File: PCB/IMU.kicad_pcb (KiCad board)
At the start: 2 copper layers, 65 parts, among them IC1 STM32F405VGT, IC2 ADP3335ARMZ-3.3, IC3 ADP3335ARMZ-5, IC4 MS5611-01BA03, P1 UART1, P2 SWD, P3 UART2, P4 SPI, P5 BATTERY, P6 USB_OTG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

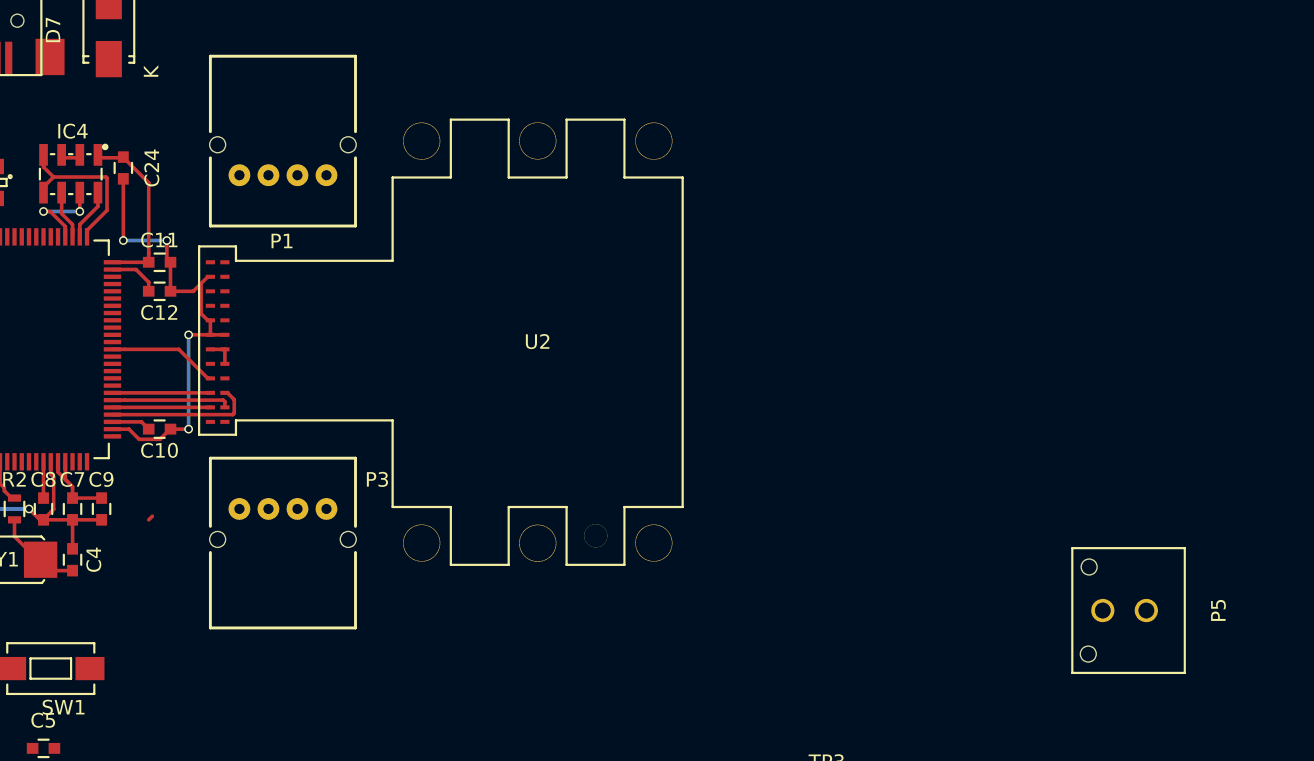
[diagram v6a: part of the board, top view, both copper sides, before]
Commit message: PCB: re-import netlist with new footprints
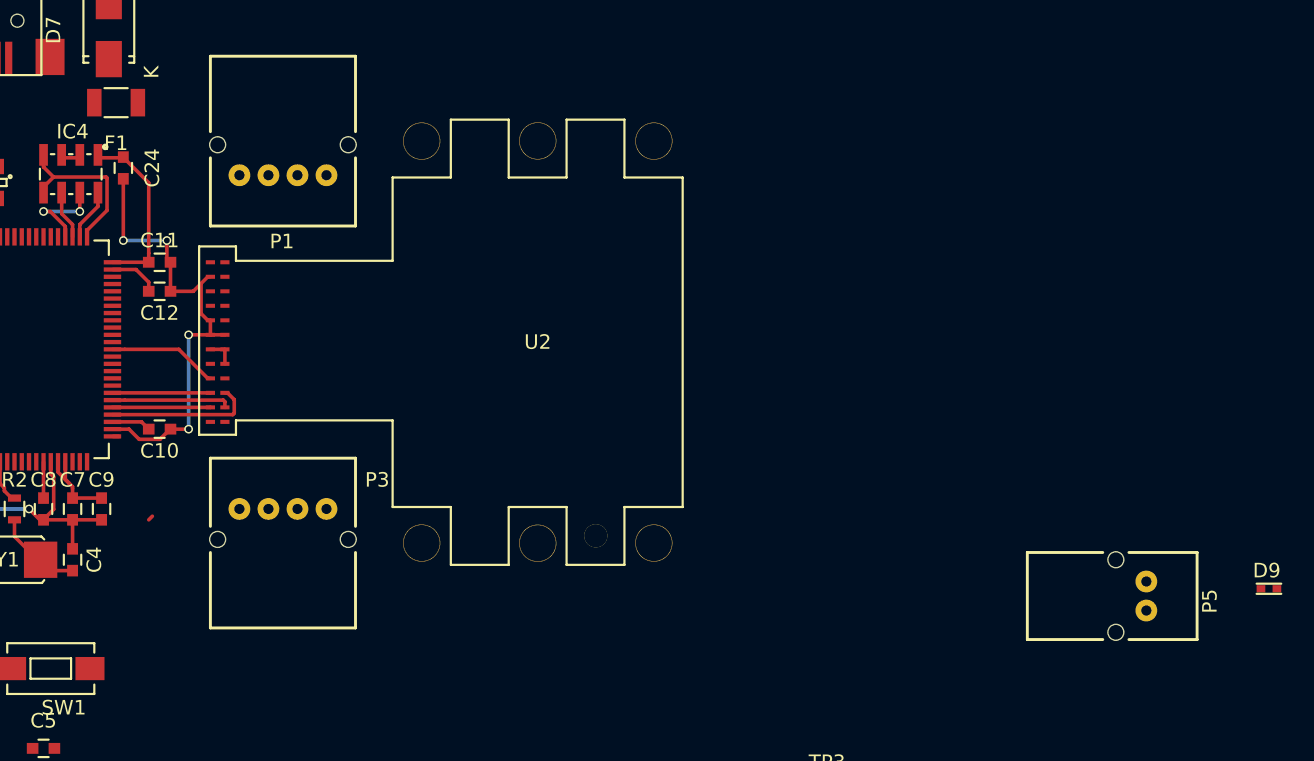
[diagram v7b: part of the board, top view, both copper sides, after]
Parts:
- added D9: CGA0402MLC-12G, IMU:R0402, F.Cu at (268.4, 119.5)
- added F1: 500mA, IMU:MC33191, F.Cu at (189.5, 86.0)
- D7: value 1N5818 -> S1A
- P5: footprint Connectors_Molex:Connector_Microfit3_Header_02x01_Straight_43045-0228 -> IMU:S02B-PASK-2
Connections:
- D7 pad 1: +5V -> +BATT
- D7 pad 2: /Power/USB5V -> Net-(D7-Pad2)
- P5 pad 1: +BATT -> Net-(D7-Pad2)
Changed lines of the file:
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@@
 (kicad_pcb (version 4) (host pcbnew 4.0.0-rc1-stable)
   (general
-    (links 181)
-    (no_connects 105)
+    (links 184)
+    (no_connects 110)
     (area 0 0 0 0)
     (thickness 1.6)
@@
     (tracks 199)
     (zones 0)
-    (modules 65)
-    (nets 122)
+    (modules 67)
+    (nets 123)
   )
   (page A4)
@@
   (net 120 "Net-(P6-Pad4)")
   (net 121 "Net-(P6-Pad6)")
+  (net 122 "Net-(D7-Pad2)")
   (net_class Default "This is the default net class."
     (clearance 0.2)
@@
     (add_net "Net-(D5-Pad2)")
     (add_net "Net-(D6-Pad2)")
+    (add_net "Net-(D7-Pad2)")
     (add_net "Net-(D8-Pad1)")
     (add_net "Net-(D8-Pad3)")
@@
       (effects (font (size 1 1) (thickness 0.15)))
     )
-    (fp_text value 1N5818 (at 0 4.3 90) (layer F.Fab)
+    (fp_text value S1A (at 0 4.3 90) (layer F.Fab)
       (effects (font (size 1 1) (thickness 0.15)))
     )
@@
     (fp_line (start -2.25044 -1.75006) (end 2.25044 -1.75006) (layer F.SilkS) (width 0.15))
     (pad 1 smd rect (at -1.99898 0 90) (size 2.49936 1.80086) (layers F.Cu F.Paste F.Mask)
-      (net 10 +5V))
+      (net 9 +BATT))
     (pad 2 smd rect (at 1.99898 0 90) (size 2.49936 1.80086) (layers F.Cu F.Paste F.Mask)
-      (net 18 /Power/USB5V))
+      (net 122 "Net-(D7-Pad2)"))
     (model Diodes_SMD.3dshapes/SMA_Standard.wrl
       (at (xyz 0 0 0))
@@
       (net 2 GND))
     (pad 8 thru_hole circle (at -9 -3 90) (size 1.6 1.6) (drill 1.1) (layers *.Cu *.Mask F.SilkS)
-      (net 2 GND))
-    (pad "" np_thru_hole circle (at 3 -3.94 90) (size 1.1 1.1) (drill 1.1) (layers *.Cu *.Mask F.SilkS))
-  )
-  (module Connectors_Molex:Connector_Microfit3_Header_02x01_Straight_43045-0228 (layer F.Cu)
-    (at 260.5 121 90)
-    (descr "Microfit3 Header Straight 02x01 43045-0228")
-    (tags "Microfit 02x01 header straight 3mm")
-    (fp_text reference P5 (at 0 5 90) (layer F.SilkS)
-      (effects (font (size 1 1) (thickness 0.15)))
-    )
-    (fp_text value BATTERY (at 0 -7 90) (layer F.Fab)
-      (effects (font (size 1 1) (thickness 0.15)))
-    )
-    (fp_line (start 4.5 2.85) (end 4.5 -5.3) (layer F.CrtYd) (width 0.05))
-    (fp_line (start 4.5 2.85) (end -4.5 2.85) (layer F.CrtYd) (width 0.05))
-    (fp_line (start -4.5 2.85) (end -4.5 -5.3) (layer F.CrtYd) (width 0.05))
-    (fp_line (start 4.5 -5.3) (end -4.5 -5.3) (layer F.CrtYd) (width 0.05))
-    (fp_line (start 4.3 2.65) (end 4.3 -5.1) (layer F.SilkS) (width 0.15))
-    (fp_line (start -4.3 2.65) (end -4.3 -5.1) (layer F.SilkS) (width 0.15))
-    (fp_line (start 4.3 2.65) (end -4.3 2.65) (layer F.SilkS) (width 0.15))
-    (fp_line (start 4.3 -5.1) (end -4.3 -5.1) (layer F.SilkS) (width 0.15))
-    (pad "" np_thru_hole circle (at -3 -4 90) (size 1.1 1.1) (drill 1.1) (layers *.Cu *.Mask F.SilkS))
-    (pad 1 thru_hole circle (at 0 0 90) (size 1.6 1.6) (drill 1.1) (layers *.Cu *.Mask F.SilkS)
-      (net 9 +BATT))
-    (pad 2 thru_hole circle (at 0 -3 90) (size 1.6 1.6) (drill 1.1) (layers *.Cu *.Mask F.SilkS)
       (net 2 GND))
     (pad "" np_thru_hole circle (at 3 -3.94 90) (size 1.1 1.1) (drill 1.1) (layers *.Cu *.Mask F.SilkS))
@@
     (pad 32 thru_hole circle (at 22.559899 -19.362802 180) (size 2.5654 2.5654) (drill 2.4892) (layers *.Cu *.Mask F.SilkS))
   )
+  (module IMU:R0402 (layer F.Cu)
+    (at 268.4 119.5)
+    (fp_text reference D9 (at 0.4 -1.25) (layer F.SilkS)
+      (effects (font (size 1 1) (thickness 0.15)))
+    )
+    (fp_text value CGA0402MLC-12G (at 0.6 1.3) (layer F.SilkS) hide
+      (effects (font (size 1 1) (thickness 0.15)))
+    )
+    (fp_line (start -0.3 0.35) (end 1.4 0.35) (layer F.SilkS) (width 0.15))
+    (fp_line (start -0.3 -0.35) (end 1.4 -0.35) (layer F.SilkS) (width 0.15))
+    (pad 1 smd rect (at 0 0) (size 0.6 0.5) (layers F.Cu F.Paste F.Mask)
+      (net 2 GND))
+    (pad 2 smd rect (at 1.1 0) (size 0.6 0.5) (layers F.Cu F.Paste F.Mask)
+      (net 122 "Net-(D7-Pad2)"))
+  )
+  (module IMU:MC33191 (layer F.Cu)
+    (at 189.5 86)
+    (fp_text reference F1 (at 0 2.8) (layer F.SilkS)
+      (effects (font (size 1 1) (thickness 0.15)))
+    )
+    (fp_text value 500mA (at 0 -2.8) (layer F.Fab)
+      (effects (font (size 1 1) (thickness 0.15)))
+    )
+    (fp_line (start -0.8 1) (end 0.8 1) (layer F.SilkS) (width 0.15))
+    (fp_line (start -0.8 -1) (end 0.8 -1) (layer F.SilkS) (width 0.15))
+    (pad 2 smd rect (at 1.5 0) (size 1 1.9) (layers F.Cu F.Paste F.Mask)
+      (net 10 +5V))
+    (pad 1 smd rect (at -1.5 0) (size 1 1.9) (layers F.Cu F.Paste F.Mask)
+      (net 18 /Power/USB5V))
+  )
+  (module IMU:S02B-PASK-2 (layer F.Cu)
+    (at 260.5 121 90)
+    (fp_text reference P5 (at 0.64 4.38 90) (layer F.SilkS)
+      (effects (font (size 1 1) (thickness 0.15)))
+    )
+    (fp_text value BATTERY (at 0.41 -7.21 90) (layer F.SilkS) hide
+      (effects (font (size 1 1) (thickness 0.15)))
+    )
+    (fp_line (start 4 -8.2) (end -2 -8.2) (layer F.SilkS) (width 0.2))
+    (fp_line (start 4 -3) (end 4 -8.2) (layer F.SilkS) (width 0.2))
+    (fp_line (start 4 3.5) (end 4 -1.2) (layer F.SilkS) (width 0.2))
+    (fp_line (start -2 3.5) (end 4 3.5) (layer F.SilkS) (width 0.2))
+    (fp_line (start -2 -1.2) (end -2 3.5) (layer F.SilkS) (width 0.2))
+    (fp_line (start -2 -8.2) (end -2 -3) (layer F.SilkS) (width 0.2))
+    (pad 1 thru_hole circle (at 0 0 90) (size 1.5 1.5) (drill 0.7) (layers *.Cu *.Mask F.SilkS)
+      (net 122 "Net-(D7-Pad2)"))
+    (pad 2 thru_hole circle (at 2 0 90) (size 1.5 1.5) (drill 0.7) (layers *.Cu *.Mask F.SilkS)
+      (net 2 GND))
+    (pad "" np_thru_hole circle (at -1.5 -2.1 90) (size 1.1 1.1) (drill 1.1) (layers *.Cu *.Mask F.SilkS))
+    (pad "" np_thru_hole circle (at 3.5 -2.1 90) (size 1.1 1.1) (drill 1.1) (layers *.Cu *.Mask F.SilkS))
+  )
+  (segment (start 191.75 114.75) (end 192 114.5) (width 0.25) (layer F.Cu) (net 0))
   (segment (start 178 113.25) (end 180.5 113.25) (width 0.25) (layer F.Cu) (net 1))
   (segment (start 190 89.75) (end 190 89.775) (width 0.25) (layer F.Cu) (net 1))
@@
   (segment (start 173.75 109) (end 171.25 109) (width 0.25) (layer F.Cu) (net 1))
   (segment (start 175.5 92.75) (end 173.5 92.75) (width 0.25) (layer F.Cu) (net 1))
-  (segment (start 191.75 114.75) (end 192 114.5) (width 0.25) (layer F.Cu) (net 2))
   (segment (start 183.5 114) (end 179.5 114) (width 0.25) (layer B.Cu) (net 2))
   (segment (start 184.5 114.75) (end 184.25 114.75) (width 0.25) (layer F.Cu) (net 2))

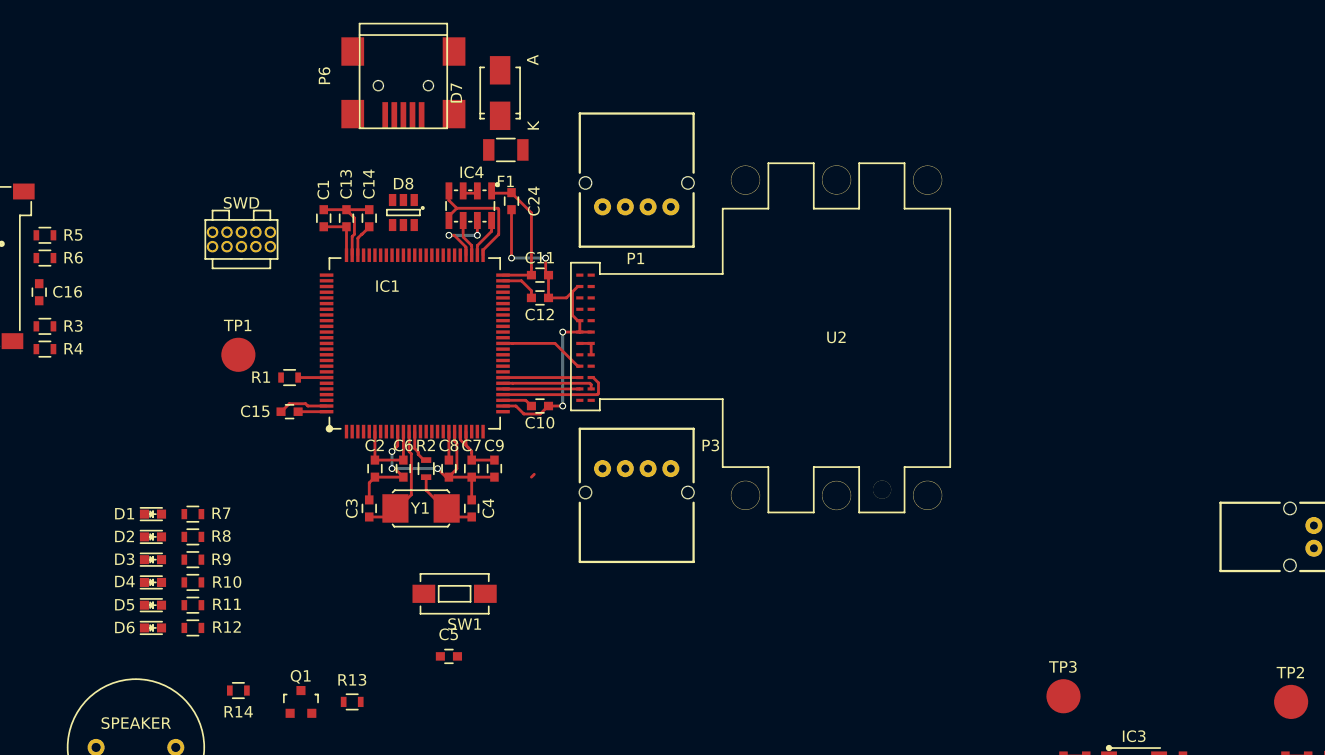
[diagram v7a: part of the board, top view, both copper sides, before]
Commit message: Update netlist and add component libraries to schematic
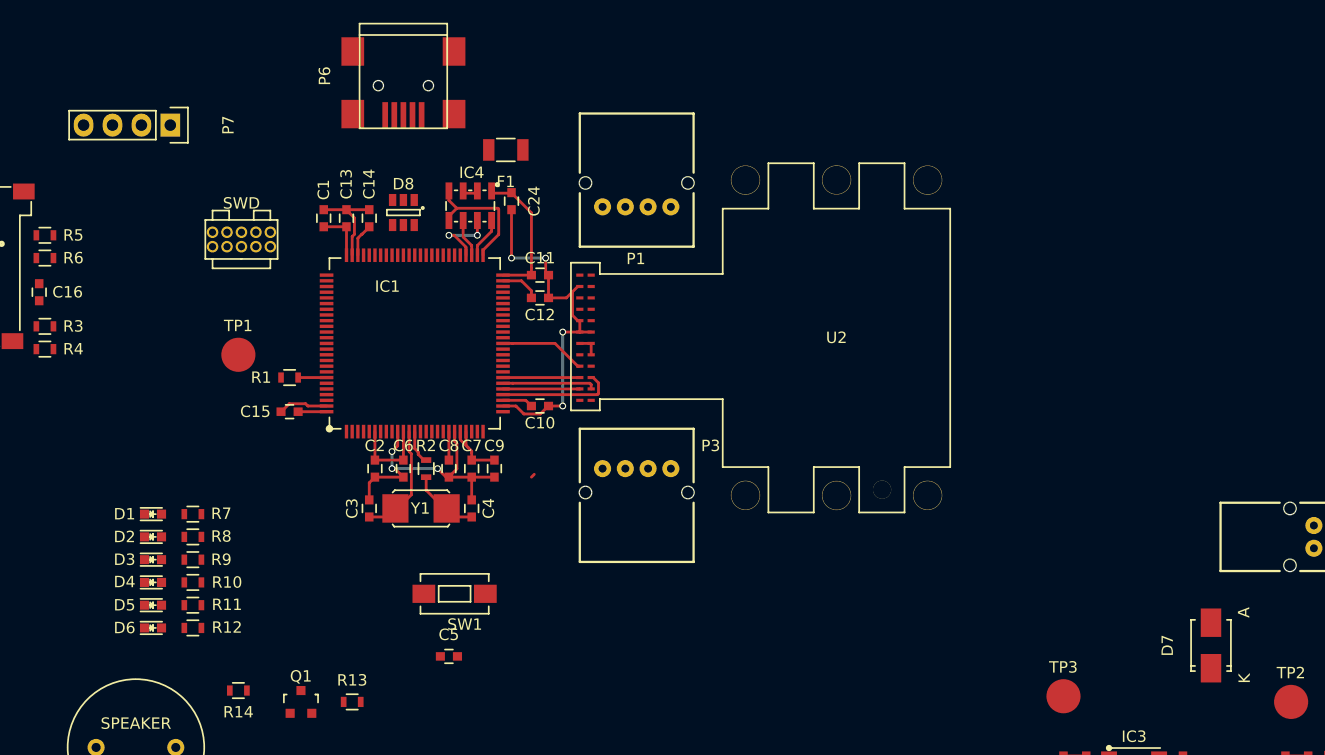
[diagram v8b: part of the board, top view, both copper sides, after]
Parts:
- added P7: CAN BUS, Pin_Headers:Pin_Header_Straight_1x04, F.Cu at (160.0, 83.8)
- moved D7 79.1 mm to (251.5, 129.5)
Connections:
- IC1 pad 81: Net-(IC1-Pad81) -> /CAN1_RX
- IC1 pad 82: Net-(IC1-Pad82) -> /CAN1_TX
